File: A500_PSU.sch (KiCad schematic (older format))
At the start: 35 parts

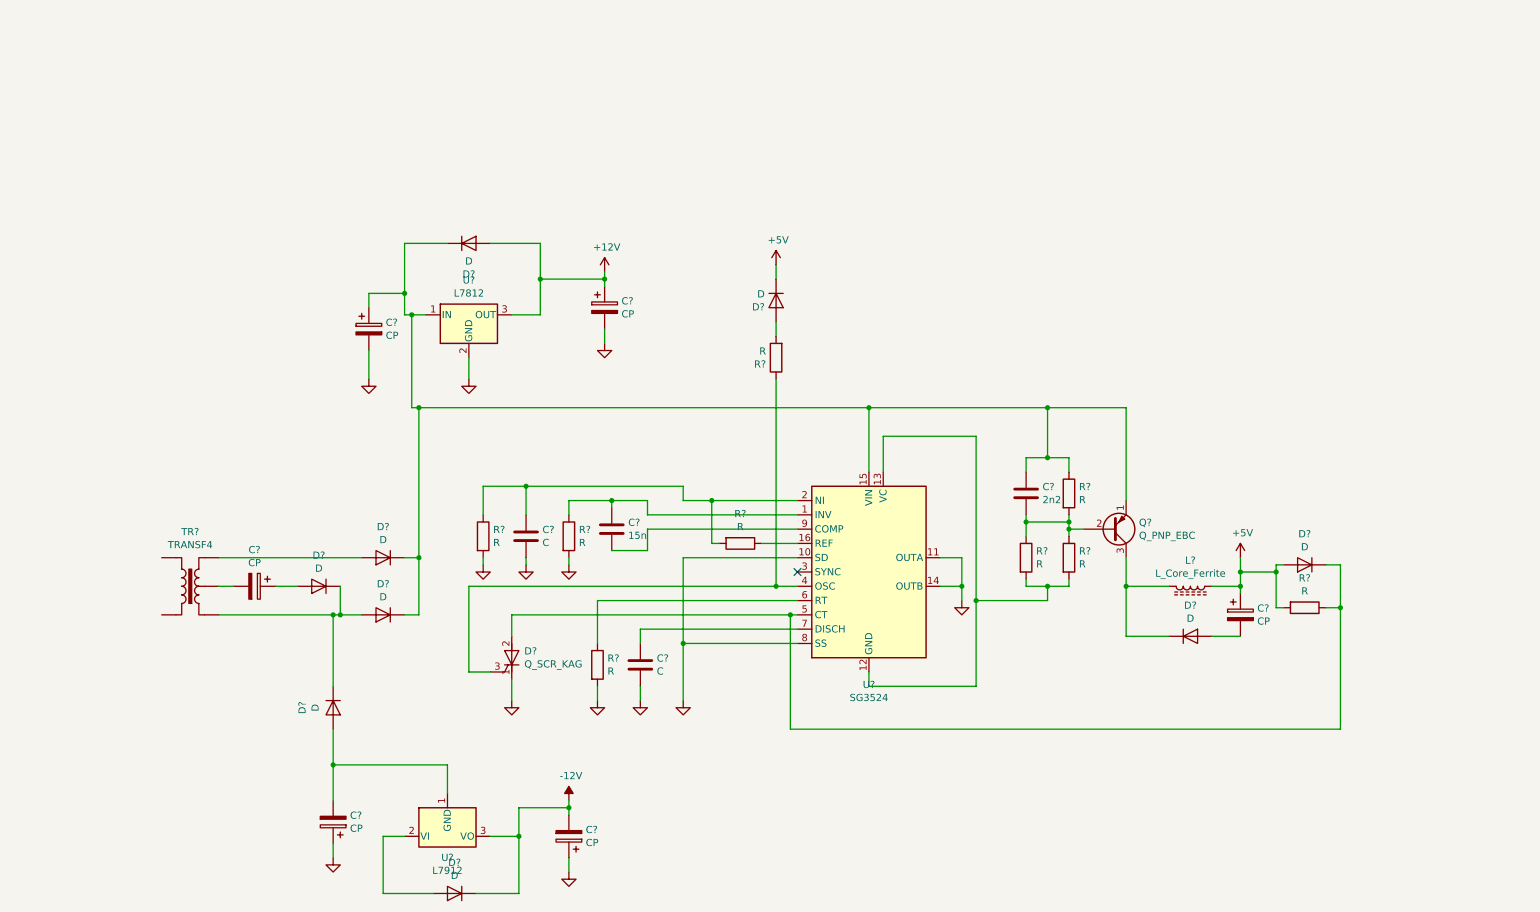
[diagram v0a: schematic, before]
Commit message: Added values for most components, fixed some errors
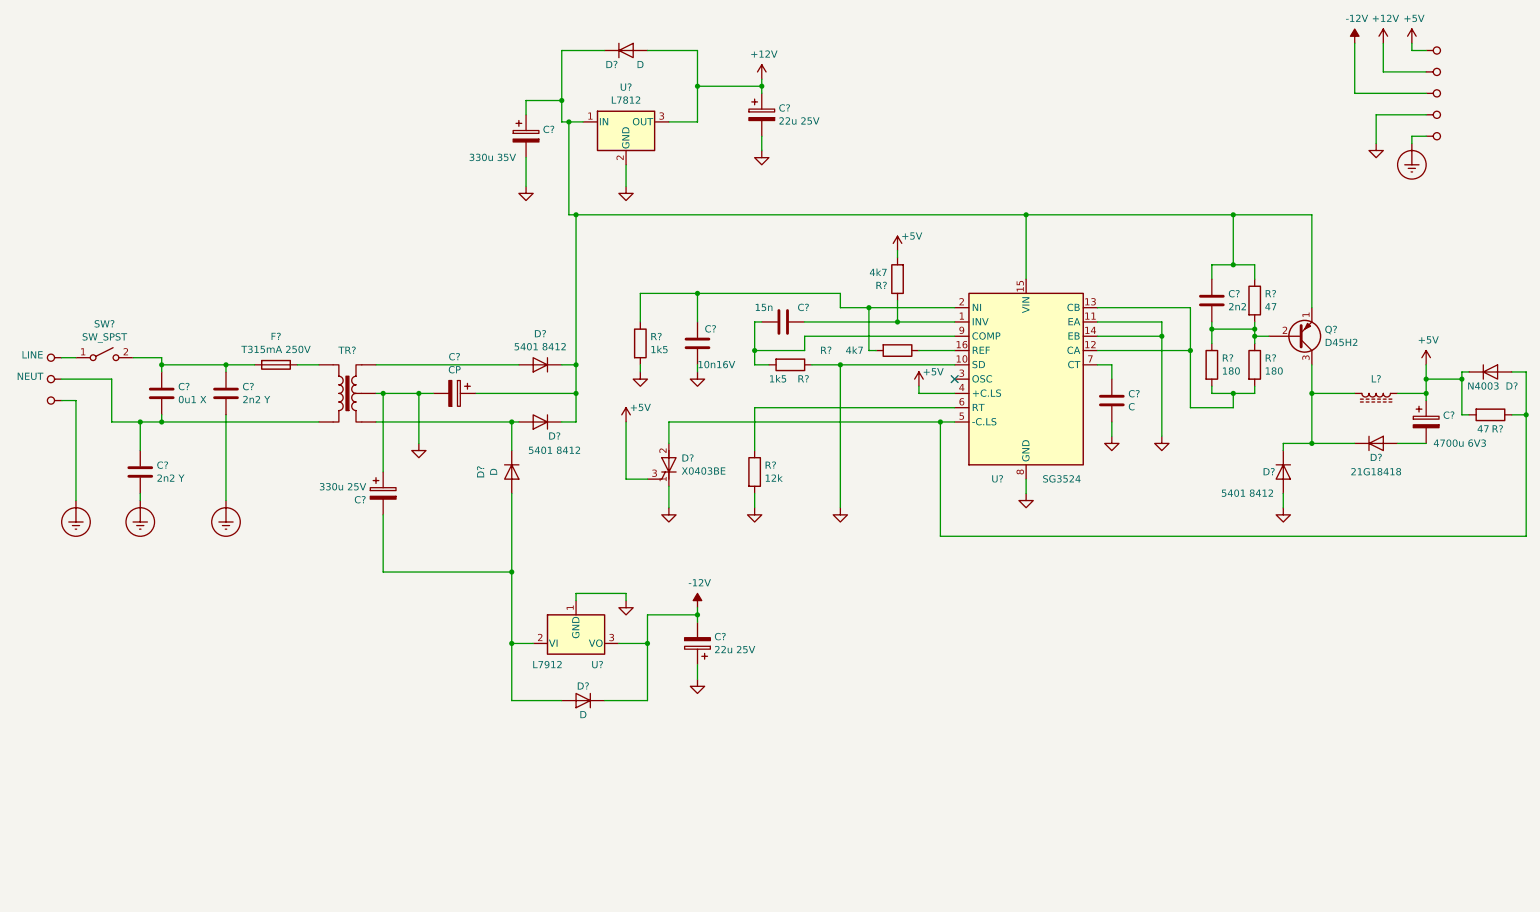
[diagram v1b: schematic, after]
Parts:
- removed D?: D, symbol Device:D
- removed R?: R, symbol Device:R
- removed U?: SG3524, symbol Regulator_Controller:SG3525
- added C?: 0u1 X, symbol Device:C
- added C? (x2): 2n2 Y, symbol Device:C
- added F?: T315mA 250V, symbol Device:Fuse
- added R?: 1k5, symbol Device:R
- added SW?: SW_SPST, symbol Switch:SW_SPST
- added U?: SG3524, symbol Regulator_Controller:SG3524
- C?: value C -> 10n16V
- C?: value CP -> 4700u 6V3
- C?: value CP -> 330u 25V
- C? (x2): value CP -> 22u 25V
- C?: value CP -> 330u 35V
- D? (x3): value D -> 5401 8412
- D?: value D -> 21G18418
- D?: value D -> N4003
- D?: value Q_SCR_KAG -> X0403BE
- Q?: value Q_PNP_EBC -> D45H2
- R?: value R -> 12k
- R? (x2): value R -> 4k7
- R?: value R -> 1k5
- R? (x2): value R -> 180
- R? (x2): value R -> 47
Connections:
- net GND is gone; now on net +12V: C?.1, C?.1, C?.2, C?.2, C?.2, C?.2, D?.1 (K), R?.2, R?.2, R?.2, U?.2 (GND)
- net +12V: now also C?.1, C?.2, C?.2, D?.1 (K), D?.1 (K), D?.2 (A), D?.3 (G), L?.1, R?.2, TR?.2, TR?.5, U?.1 (GND), U?.3 (VO), C?.1, C?.2, C?.2, C?.2, R?.1, U?.10 (SD), U?.11 (EA), U?.14 (EB), U?.4 (+C.LS), U?.8 (GND)
- net at D?.1 (K), D?.2 (A), TR?.1: no longer D?.1 (K)
- net at TR?.4: now also F?.1
- net at C?.1, C?.1, D?.1 (K)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: now also C?.1, U?.15 (VIN)
- net at C?.1, R?.1: now also U?.1 (INV)
- net at R?.2, R?.2: now also U?.12 (CA), U?.13 (CB)
- net at R?.1: now also U?.16 (REF)
- net at C?.1, R?.1, R?.2: now also U?.2 (NI)
- net at D?.2 (A), R?.1: now also D?.2 (A), U?.5 (-C.LS); no longer D?.1 (K)
- net at R?.1: now also U?.6 (RT)
- net at C?.1: now also U?.7 (CT)
- net at C?.2: now also R?.2, U?.9 (COMP)
- net at D?.1 (K), L?.2, Q?.3 (C): now also D?.1 (K)
- net at D?.2 (A), U?.2 (VI): now also C?.2, D?.2 (A)
- removed net +5V: C?.1, D?.2 (A), L?.1, R?.2
- removed net -12V: C?.2, D?.1 (K), U?.3 (VO)
- new net: C?.1, C?.1, F?.2, SW?.2 (B)
- new net LINE: SW?.1 (A)
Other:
- moved on the sheet: C?, D?, L?, Q?, R?, TR?, U?

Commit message: tidied up and added schematic info
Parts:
- C?: value CP -> 4700u 25V
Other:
- moved on the sheet: C?, D?, F?, L?, Q?, R?, SW?, TR?, U?

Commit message: Added pdf schematic
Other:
- note added: "INPUT \n220V 50Hz 0.3A\nOUTPUT \n5V=2.5A\n12V=1.0A\n-12V=0.1A"
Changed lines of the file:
@@
 Wire Wire Line
 	10050 3050 9850 3050
+Text Notes 2300 2650 0    118  ~ 0
+INPUT \n220V 50Hz 0.3A\nOUTPUT \n5V=2.5A\n12V=1.0A\n-12V=0.1A
 $EndSCHEMATC

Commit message: fixed some errors in the error amplifier input circuit
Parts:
- gave numbers to parts that had none: 39
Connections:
- net at C8.1, R4.1, U2.1 (INV): now also R2.2
- net at C8.2, U2.9 (COMP): no longer R2.2
- net at C6.1, R1.1, U2.2 (NI): now also R5.1; no longer R5.2
- net at U2.16 (REF): now also R5.2; no longer R5.1
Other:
- moved on the sheet: C6, C8, D5, R1, R2, R3, R4, R5

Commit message: More errors fixed
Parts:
- removed Q1: D45H2, symbol Device:Q_PNP_EBC
- added D10: D, symbol Device:D
- added Q1: D45H2, symbol Device:Q_PNP_BCE
- added R10, R11: 47, symbol Device:R
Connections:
- net +12V: now also D9.2 (A), R10.2, R11.1; no longer D5.3 (G), D9.1 (K)
- net at C12.1, C4.1, C9.1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: now also Q1.3 (E)
- net at C12.2, R6.1, R7.2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: now also Q1.1 (B)
- net at D7.1 (K), D8.1 (K), L1.2: now also Q1.2 (C)
- net at D5.2 (A), R9.1, U2.5 (-C.LS): now also D9.1 (K); no longer D9.2 (A)
- new net: D10.2 (A), D5.3 (G), R11.2
- new net: D10.1 (K), R10.1
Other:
- moved on the sheet: C12, R7
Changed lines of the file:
@@
 L Device:R R7
 U 1 1 5E632579
-P 8700 3600
-F 0 "R7" H 8770 3646 50  0000 L CNN
-F 1 "47" H 8770 3555 50  0000 L CNN
-F 2 "" V 8630 3600 50  0001 C CNN
-F 3 "~" H 8700 3600 50  0001 C CNN
-	1    8700 3600
+P 8800 3350
+F 0 "R7" H 8870 3396 50  0000 L CNN
+F 1 "47" H 8870 3305 50  0000 L CNN
+F 2 "" V 8730 3350 50  0001 C CNN
+F 3 "~" H 8800 3350 50  0001 C CNN
+	1    8800 3350
 	1    0    0    -1
 $EndComp
@@
 L Device:C C12
 U 1 1 5E632A41
-P 8400 3600
-F 0 "C12" H 8515 3646 50  0000 L CNN
-F 1 "2n2" H 8515 3555 50  0000 L CNN
-F 2 "" H 8438 3450 50  0001 C CNN
-F 3 "~" H 8400 3600 50  0001 C CNN
-	1    8400 3600
+P 8400 3350
+F 0 "C12" H 8515 3396 50  0000 L CNN
+F 1 "2n2" H 8515 3305 50  0000 L CNN
+F 2 "" H 8438 3200 50  0001 C CNN
+F 3 "~" H 8400 3350 50  0001 C CNN
+	1    8400 3350
 	1    0    0    -1
 $EndComp
@@
 Connection ~ 8550 4250
 Wire Wire Line
-	8700 3900 8700 3850
-Wire Wire Line
-	8400 3900 8400 3800
-Wire Wire Line
-	8400 3450 8400 3350
-Wire Wire Line
-	8400 3350 8550 3350
-Wire Wire Line
-	8700 3350 8700 3450
-Wire Wire Line
-	8550 3350 8550 3000
-Wire Wire Line
 	7350 3000 7350 3450
-Connection ~ 8550 3350
-Wire Wire Line
-	8550 3350 8700 3350
 Wire Wire Line
 	4100 4450 4200 4450
@@
 Connection ~ 4200 4050
 Wire Wire Line
-	8400 3800 8700 3800
-Connection ~ 8400 3800
-Wire Wire Line
-	8400 3800 8400 3750
-Connection ~ 8700 3800
-Wire Wire Line
-	8700 3800 8700 3750
-$Comp
-L Device:Q_PNP_EBC Q1
-U 1 1 5E63D87F
-P 9000 3850
-F 0 "Q1" H 9190 3804 50  0000 L CNN
-F 1 "D45H2" H 9190 3895 50  0000 L CNN
-F 2 "" H 9200 3950 50  0001 C CNN
-F 3 "~" H 9000 3850 50  0001 C CNN
-	1    9000 3850
-	1    0    0    1
-$EndComp
-Wire Wire Line
-	8800 3850 8700 3850
-Connection ~ 8700 3850
-Wire Wire Line
-	8700 3850 8700 3800
-Wire Wire Line
 	4200 3000 7150 3000
-Wire Wire Line
-	9100 3650 9100 3000
-Wire Wire Line
-	9100 3000 8550 3000
-Connection ~ 8550 3000
 $Comp
 L Device:D D8
@@
 $EndComp
 Wire Wire Line
-	9400 4600 9100 4600
-Wire Wire Line
-	9400 4250 9100 4250
-Wire Wire Line
-	9100 4250 9100 4050
+	9400 4600 9200 4600
+Wire Wire Line
+	9400 4250 9200 4250
 $Comp
 L Device:CP C13
@@
 F 3 "~" H 10350 4100 50  0001 C CNN
 	1    10350 4100
-	1    0    0    -1
+	-1   0    0    1
 $EndComp
 $Comp
@@
 U 1 1 5E67B970
 P 10350 4400
-F 0 "R9" V 10450 4450 50  0000 C CNN
+F 0 "R9" V 10450 4500 50  0000 C CNN
 F 1 "47" V 10450 4350 50  0000 C CNN
 F 2 "" V 10280 4400 50  0001 C CNN
@@
 Wire Wire Line
 	6750 5250 6750 5400
-Wire Wire Line
-	6600 5650 6550 5650
-Wire Wire Line
-	6550 5650 6550 5500
 $Comp
 L power:GND #PWR015
@@
 Wire Wire Line
 	7950 4050 7850 4050
-Wire Wire Line
-	7350 3000 8550 3000
 Connection ~ 7350 3000
 Wire Wire Line
@@
 L power:+5V #PWR014
 U 1 1 5E6A8F93
-P 6550 5500
-F 0 "#PWR014" H 6550 5350 50  0001 C CNN
-F 1 "+5V" H 6650 5600 50  0000 C CNN
-F 2 "" H 6550 5500 50  0001 C CNN
-F 3 "" H 6550 5500 50  0001 C CNN
-	1    6550 5500
+P 4900 7000
+F 0 "#PWR014" H 4900 6850 50  0001 C CNN
+F 1 "+5V" H 5000 7100 50  0000 C CNN
+F 2 "" H 4900 7000 50  0001 C CNN
+F 3 "" H 4900 7000 50  0001 C CNN
+	1    4900 7000
 	1    0    0    -1
 $EndComp
@@
 	6850 4450 6750 4450
 Wire Wire Line
-	9100 4600 9100 4250
-Connection ~ 9100 4250
+	9200 4600 9200 4250
 Wire Wire Line
 	6750 5250 6750 4450
@@
 	4200 4250 4200 4050
 Wire Wire Line
-	9100 4600 8900 4600
+	9200 4600 8900 4600
 Wire Wire Line
 	8900 4600 8900 4650
-Connection ~ 9100 4600
+Connection ~ 9200 4600
 $Comp
 L power:GND #PWR027
@@
 INPUT \n220V 50Hz 0.3A\nOUTPUT \n5V=2.5A\n12V=1.0A\n-12V=0.1A
 $Comp
-L power:GND #PWR?
+L power:GND #PWR039
 U 1 1 5E64ADCD
 P 5500 4250
-F 0 "#PWR?" H 5500 4000 50  0001 C CNN
+F 0 "#PWR039" H 5500 4000 50  0001 C CNN
 F 1 "GND" H 5505 4077 50  0001 C CNN
 F 2 "" H 5500 4250 50  0001 C CNN
@@
 	5200 3650 6150 3650
 Connection ~ 6750 5250
+Wire Wire Line
+	8700 3900 8700 3800
+Wire Wire Line
+	8700 3800 8400 3800
+Wire Wire Line
+	8400 3800 8400 3900
+Wire Wire Line
+	8700 3800 8800 3800
+Connection ~ 8700 3800
+Wire Wire Line
+	7350 3000 8400 3000
+Wire Wire Line
+	8400 3200 8400 3000
+Connection ~ 8400 3000
+Wire Wire Line
+	8400 3000 8800 3000
+Wire Wire Line
+	8400 3500 8400 3800
+Connection ~ 8400 3800
+Wire Wire Line
+	8800 3800 8800 3500
+Connection ~ 8800 3800
+Wire Wire Line
+	8800 3800 8900 3800
+Wire Wire Line
+	8800 3200 8800 3000
+Connection ~ 8800 3000
+Wire Wire Line
+	8800 3000 9200 3000
+$Comp
+L Device:Q_PNP_BCE Q1
+U 1 1 5E722C66
+P 9100 3800
+F 0 "Q1" H 9291 3754 50  0000 L CNN
+F 1 "D45H2" H 9291 3845 50  0000 L CNN
+F 2 "" H 9300 3900 50  0001 C CNN
+F 3 "~" H 9100 3800 50  0001 C CNN
+	1    9100 3800
+	1    0    0    1
+$EndComp
+Wire Wire Line
+	9200 4000 9200 4250
+Connection ~ 9200 4250
+Wire Wire Line
+	9200 3600 9200 3000
+$Comp
+L power:+5V #PWR040
+U 1 1 5E79567E
+P 6150 4750
+F 0 "#PWR040" H 6150 4600 50  0001 C CNN
+F 1 "+5V" H 6165 4923 50  0000 C CNN
+F 2 "" H 6150 4750 50  0001 C CNN
+F 3 "" H 6150 4750 50  0001 C CNN
+	1    6150 4750
+	1    0    0    -1
+$EndComp
+$Comp
+L Device:R R10
+U 1 1 5E795A89
+P 6150 4950
+F 0 "R10" H 6300 4950 50  0000 C CNN
+F 1 "47" H 6050 4950 50  0000 C CNN
+F 2 "" V 6080 4950 50  0001 C CNN
+F 3 "~" H 6150 4950 50  0001 C CNN
+	1    6150 4950
+	-1   0    0    1
+$EndComp
+$Comp
+L Device:D D10
+U 1 1 5E796279
+P 6150 5300
+F 0 "D10" V 6100 5150 50  0000 C CNN
+F 1 "D" V 6200 5200 50  0000 C CNN
+F 2 "" H 6150 5300 50  0001 C CNN
+F 3 "~" H 6150 5300 50  0001 C CNN
+	1    6150 5300
+	0    1    1    0
+$EndComp
+Wire Wire Line
+	6150 4750 6150 4800
+Wire Wire Line
+	6150 5100 6150 5150
+Wire Wire Line
+	6150 5450 6150 5650
+Wire Wire Line
+	6150 5650 6600 5650
+$Comp
+L Device:R R11
+U 1 1 5E7D3F39
+P 6150 5850
+F 0 "R11" H 6250 6000 50  0000 C CNN
+F 1 "47" H 6250 5850 50  0000 C CNN
+F 2 "" V 6080 5850 50  0001 C CNN
+F 3 "~" H 6150 5850 50  0001 C CNN
+	1    6150 5850
+	-1   0    0    1
+$EndComp
+$Comp
+L power:GND #PWR041
+U 1 1 5E7D43AD
+P 6150 6100
+F 0 "#PWR041" H 6150 5850 50  0001 C CNN
+F 1 "GND" H 6155 5927 50  0001 C CNN
+F 2 "" H 6150 6100 50  0001 C CNN
+F 3 "" H 6150 6100 50  0001 C CNN
+	1    6150 6100
+	1    0    0    -1
+$EndComp
+Wire Wire Line
+	6150 6100 6150 6000
+Wire Wire Line
+	6150 5700 6150 5650
+Connection ~ 6150 5650
 $EndSCHEMATC
